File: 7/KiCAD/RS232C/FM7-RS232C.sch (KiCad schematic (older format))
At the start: 31 parts, among them CN2 DB9_Male, M10 74LS04, M11 8251A, M12 74LS27, M13 74LS11, M2 74LS38, M3 75188, M4 75189, M5 74LS00, M6 74LS32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

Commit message: Rewiring to add COM0/COM2 choice.
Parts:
- added unit 1 of M5
- added unit 1 of M6
- M6: footprint Package_DIP:DIP-14_W7.62mm_Socket -> (none)
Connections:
- net +5V: no longer M13.11
- net GNDPWR: now also M12.3; no longer M12.13
- net ~EIOS: now also M12.10; no longer M12.9
- net EAB0: now reaches CN_A1.1 (Pin_1), M11.12 (C/~D), M6.10
- net EAB2: now reaches CN_A1.2 (Pin_2), M13.1, M6.9
- net EAB4: now reaches CN_A1.3 (Pin_3), M12.2
- net EAB6: now reaches CN_A1.4 (Pin_4), M12.4
- net EAB6: now also M6.2
- net EAB1: now reaches CN_B1.1 (Pin_1), M13.2, M7.5
- net EAB1: now also M7.4
- net EAB3: now reaches CN_B1.2 (Pin_2), M12.1
- net EAB5: now reaches CN_B1.3 (Pin_3), M12.5
- net EAB5: now also M6.1
- net EAB7: now reaches CN_B1.4 (Pin_4)
- net EAB7: now also M12.13; no longer M12.3
- net at M6.8: now also M12.9; no longer M12.11
- net at M7.6: now also M12.11; no longer M12.10
- net at M13.12: now also M13.5; no longer M13.4
- removed net AB34: M12.12, M13.3, M7.4
- removed net AB567: M12.6, M13.5, M7.3
- net ~ERQ renamed ~ERW
- net ~ERW: now also M13.11; no longer M7.1
- new net: M5.3, M7.1
- new net: M5.1, M5.2, M6.3
- new net AB347: M12.12, M13.4, M7.3
- new net AB56: M12.6, M13.3
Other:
- note added: "+5V"
- note added: "=0 if AB02=0"
- note added: "=0 if IOS (FDxx)"
- note added: "=0\nif AB347=0,AB0=1"
- note added: "AB1=1"
- note added: "AB347=0"
- note added: "AB56=0"
- note added: "All Input=1 \nif FD02"
- note added: "GND"
- moved on the sheet: M7B
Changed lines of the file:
@@
 EESchema Schematic File Version 4
-LIBS:FM7-RS232C-cache
-EELAYER 26 0
+EELAYER 30 0
 EELAYER END
 $Descr A0 46811 33110
@@
 F 0 "M6" H 11100 9525 50  0000 C CNN
 F 1 "74LS32" H 11100 9434 50  0000 C CNN
-F 2 "Package_DIP:DIP-14_W7.62mm_Socket" H 11100 9200 50  0001 C CNN
+F 2 "" H 11100 9200 50  0001 C CNN
 F 3 "http://www.ti.com/lit/gpn/sn74LS32" H 11100 9200 50  0001 C CNN
 	3    11100 9200
@@
 L 74xx:74LS10 M7
 U 2 1 5C0782CB
-P 11100 9900
-F 0 "M7" H 11100 10225 50  0000 C CNN
-F 1 "74LS10" H 11100 10134 50  0000 C CNN
-F 2 "Package_DIP:DIP-14_W7.62mm_Socket" H 11100 9900 50  0001 C CNN
-F 3 "http://www.ti.com/lit/gpn/sn74LS10" H 11100 9900 50  0001 C CNN
-	2    11100 9900
+P 11100 10000
+F 0 "M7" H 11100 10325 50  0000 C CNN
+F 1 "74LS10" H 11100 10234 50  0000 C CNN
+F 2 "Package_DIP:DIP-14_W7.62mm_Socket" H 11100 10000 50  0001 C CNN
+F 3 "http://www.ti.com/lit/gpn/sn74LS10" H 11100 10000 50  0001 C CNN
+	2    11100 10000
 	1    0    0    -1
 $EndComp
@@
 F 0 "M6" H 11100 11825 50  0000 C CNN
 F 1 "74LS32" H 11100 11734 50  0000 C CNN
-F 2 "Package_DIP:DIP-14_W7.62mm_Socket" H 11100 11500 50  0001 C CNN
+F 2 "" H 11100 11500 50  0001 C CNN
 F 3 "http://www.ti.com/lit/gpn/sn74LS32" H 11100 11500 50  0001 C CNN
 	4    11100 11500
@@
 +5V
 Wire Wire Line
-	11400 9900 11750 9900
-Wire Wire Line
 	12350 9900 12600 9900
 Wire Wire Line
@@
 	12550 10000 12600 10000
 Wire Wire Line
-	8050 10600 10700 10600
-Wire Wire Line
-	5100 10500 10550 10500
-Wire Wire Line
-	10550 10500 10550 11600
-Wire Wire Line
-	10550 11600 10800 11600
-Connection ~ 10550 10500
-Wire Wire Line
-	10550 10500 10800 10500
-Wire Wire Line
-	10700 10600 10700 11400
-Wire Wire Line
-	10700 11400 10800 11400
-Connection ~ 10700 10600
-Wire Wire Line
-	10700 10600 10800 10600
-Wire Wire Line
-	10350 18600 10350 10700
-Wire Wire Line
-	10350 10700 10800 10700
-Wire Wire Line
-	11400 9200 11450 9200
-Wire Wire Line
-	11450 9200 11450 10000
-Wire Wire Line
-	11450 10000 11750 10000
+	8050 10600 10550 10600
+Wire Wire Line
+	5100 10500 10300 10500
+Wire Wire Line
+	10300 10500 10300 11600
+Wire Wire Line
+	10300 11600 10800 11600
+Connection ~ 10300 10500
+Wire Wire Line
+	10300 10500 10800 10500
+Wire Wire Line
+	10550 10600 10550 11400
+Wire Wire Line
+	10550 11400 10800 11400
+Connection ~ 10550 10600
+Wire Wire Line
+	10550 10600 10800 10600
+Wire Wire Line
+	11400 9200 11650 9200
+Wire Wire Line
+	11650 9200 11650 9800
 Wire Wire Line
 	3700 11600 4100 11600
@@
 Wire Wire Line
 	6950 11900 6950 8050
-Text Notes 6950 6650 0    50   ~ 0
+Text Notes 6950 6700 0    50   ~ 0
 EAB0
-Text Notes 6950 6850 0    50   ~ 0
+Text Notes 6950 6900 0    50   ~ 0
 EAB2
-Text Notes 6950 7050 0    50   ~ 0
+Text Notes 6950 7100 0    50   ~ 0
 EAB4
-Text Notes 6950 7250 0    50   ~ 0
+Text Notes 6950 7300 0    50   ~ 0
 EAB6
-Text Notes 7000 7450 0    50   ~ 0
+Text Notes 7600 7450 0    50   ~ 0
 EAB1
-Text Notes 7000 7650 0    50   ~ 0
+Text Notes 7600 7650 0    50   ~ 0
 EAB3
-Text Notes 7000 7850 0    50   ~ 0
+Text Notes 7600 7850 0    50   ~ 0
 EAB5
-Text Notes 7000 8050 0    50   ~ 0
+Text Notes 7600 8050 0    50   ~ 0
 EAB7
 Wire Wire Line
@@
 	4800 12800 4800 17500
 Wire Wire Line
-	8750 7450 8750 10000
-Wire Wire Line
-	8750 10000 10800 10000
-Connection ~ 10350 18600
+	8750 7450 8750 10100
+Wire Wire Line
+	8750 10100 10650 10100
 Wire Wire Line
 	6850 18600 7700 18600
@@
 Wire Wire Line
 	5200 9450 11550 9450
-Wire Wire Line
-	11550 9450 11550 9800
-Wire Wire Line
-	11550 9800 11750 9800
 Connection ~ 7400 19700
 Connection ~ 11500 19700
@@
 	12300 6700 14700 6700
 Wire Wire Line
-	6900 7850 12300 7850
-Wire Wire Line
-	12400 8050 12400 6500
-Wire Wire Line
-	12400 6500 14700 6500
-Wire Wire Line
-	6950 8050 12400 8050
+	6900 7850 9800 7850
+Wire Wire Line
+	12750 8050 12750 7200
+Wire Wire Line
+	6950 8050 12750 8050
 Wire Wire Line
 	12200 7300 12200 6600
@@
 	12200 6600 14700 6600
 Wire Wire Line
-	4250 7300 12200 7300
+	4250 7300 9400 7300
 Wire Wire Line
 	12600 7650 12600 7000
 Wire Wire Line
 	6850 7650 12600 7650
-Wire Wire Line
-	13850 7200 13850 19700
 Connection ~ 13850 19700
 Wire Wire Line
@@
 Wire Wire Line
 	9100 6900 13550 6900
-Wire Wire Line
-	14700 7200 13850 7200
 Wire Wire Line
 	12600 7000 14700 7000
@@
 	15300 7100 15400 7100
 Wire Wire Line
-	15400 7100 15400 7550
-Wire Wire Line
-	15400 7550 15750 7550
+	15400 7100 15400 7650
 Wire Wire Line
 	15300 6600 15650 6600
 Wire Wire Line
-	15650 6600 15650 7750
-Wire Wire Line
-	15650 7750 15750 7750
+	15650 6600 15650 7550
 Wire Wire Line
 	15400 7100 15400 4200
 Connection ~ 15400 7100
 Wire Wire Line
-	15650 6600 15650 3900
-Connection ~ 15650 6600
-Wire Wire Line
 	15250 8100 15400 8100
 Wire Wire Line
-	15400 8100 15400 7650
-Wire Wire Line
-	15400 7650 15750 7650
+	15400 8100 15400 7750
 Wire Wire Line
 	15400 4200 10500 4200
-Wire Wire Line
-	15650 3900 10100 3900
-Wire Wire Line
-	10100 3900 10100 9800
-Text Label 13450 3900 0    50   ~ 0
-AB567
+Text Label 15650 6800 0    50   ~ 0
+AB56
 Text Label 13450 4200 0    50   ~ 0
-AB34
-Wire Wire Line
-	10100 9800 10800 9800
+AB347
 Wire Wire Line
 	10500 4200 10500 9900
@@
 	16250 11850 16900 11850
 Wire Wire Line
-	16250 11850 16250 9050
-Wire Wire Line
-	16250 9050 12400 9050
-Wire Wire Line
-	12400 9050 12400 9800
-Wire Wire Line
-	12400 9800 12600 9800
+	16250 11850 16250 10600
+Wire Wire Line
+	16250 10600 13200 10600
+Wire Wire Line
+	12550 9800 12600 9800
 Connection ~ 16250 11850
-Text Label 15250 9050 0    50   ~ 0
-~ERQ
+Text Label 15250 10600 0    50   ~ 0
+~ERW
 $Comp
 L 74xx:74LS04 M10
@@
 	7600 16250 15600 16250
 Connection ~ 7500 12300
-Wire Wire Line
-	13200 9900 13500 9900
-Wire Wire Line
-	13500 9900 13500 16450
 Text Label 13250 9900 0    50   ~ 0
 ~WFD02
-Wire Wire Line
-	13500 16450 15600 16450
 Wire Wire Line
 	11400 11500 16900 11500
@@
 F 0 "M6" H 9430 19246 50  0000 L CNN
 F 1 "74LS32" H 9430 19155 50  0000 L CNN
-F 2 "Package_DIP:DIP-14_W7.62mm_Socket" H 9200 19200 50  0001 C CNN
+F 2 "" H 9200 19200 50  0001 C CNN
 F 3 "http://www.ti.com/lit/gpn/sn74LS32" H 9200 19200 50  0001 C CNN
 	5    9200 19200
@@
 	9200 18600 10000 18600
 Connection ~ 10000 18600
-Wire Wire Line
-	10000 18600 10350 18600
-Wire Wire Line
-	10350 18600 10750 18600
 Connection ~ 10750 19700
 Wire Wire Line
@@
 Text Label 7050 12400 0    50   ~ 0
 EE
+Text Label 6600 6700 0    50   ~ 0
+EAB0
+Text Label 6600 6900 0    50   ~ 0
+EAB2
+Text Label 6600 7100 0    50   ~ 0
+EAB4
+Text Label 6600 7300 0    50   ~ 0
+EAB6
+Text Label 7050 7450 0    50   ~ 0
+EAB1
+Text Label 7050 7650 0    50   ~ 0
+EAB3
+Text Label 7050 7850 0    50   ~ 0
+EAB5
+Text Label 7050 8050 0    50   ~ 0
+EAB7
+Text Notes 14550 8300 0    50   ~ 0
++5V
+Text Notes 14050 6500 0    50   ~ 0
+GND
+Wire Wire Line
+	12750 7200 14700 7200
+Wire Wire Line
+	14700 6500 13850 6500
+Wire Wire Line
+	13850 6500 13850 19700
+Wire Wire Line
+	15650 7550 15750 7550
+Wire Wire Line
+	15400 7650 15750 7650
+Wire Wire Line
+	15400 7750 15750 7750
+Wire Wire Line
+	11750 9800 11650 9800
+Wire Wire Line
+	11550 9900 11750 9900
+Wire Wire Line
+	11550 9450 11550 9900
+Wire Wire Line
+	11400 10000 11750 10000
+Text Notes 10500 9900 0    50   ~ 0
+AB347=0
+Text Notes 10300 10100 0    50   ~ 0
+AB1=1
+Text Notes 11300 10150 0    50   ~ 0
+=0\nif AB347=0,AB0=1
+Text Notes 11400 9200 0    50   ~ 0
+=0 if AB02=0
+Text Notes 10750 9450 0    50   ~ 0
+=0 if IOS (FDxx)
+Wire Wire Line
+	13700 9900 13700 16450
+Wire Wire Line
+	13200 9900 13700 9900
+Wire Wire Line
+	13700 16450 15600 16450
+Text Notes 12750 10250 0    50   ~ 0
+All Input=1 \nif FD02
+Wire Wire Line
+	13200 10600 13200 10950
+Wire Wire Line
+	13200 10950 10750 10950
+Wire Wire Line
+	10000 18600 10750 18600
+Wire Wire Line
+	10750 10700 10800 10700
+Wire Wire Line
+	10750 10700 10750 10950
+$Comp
+L 74xx:74LS32 M6
+U 1 1 621B650C
+P 11100 8550
+F 0 "M6" H 11100 8875 50  0000 C CNN
+F 1 "74LS32" H 11100 8784 50  0000 C CNN
+F 2 "" H 11100 8550 50  0001 C CNN
+F 3 "http://www.ti.com/lit/gpn/sn74LS32" H 11100 8550 50  0001 C CNN
+	1    11100 8550
+	1    0    0    -1
+$EndComp
+$Comp
+L 74xx:74LS00 M5
+U 1 1 621B9524
+P 12050 8550
+F 0 "M5" H 12050 8875 50  0000 C CNN
+F 1 "74LS00" H 12050 8784 50  0000 C CNN
+F 2 "" H 12050 8550 50  0001 C CNN
+F 3 "http://www.ti.com/lit/gpn/sn74ls00" H 12050 8550 50  0001 C CNN
+	1    12050 8550
+	1    0    0    -1
+$EndComp
+Wire Wire Line
+	11400 8550 11600 8550
+Wire Wire Line
+	11600 8550 11600 8450
+Wire Wire Line
+	11600 8450 11750 8450
+Wire Wire Line
+	11600 8550 11600 8650
+Wire Wire Line
+	11600 8650 11750 8650
+Connection ~ 11600 8550
+Wire Wire Line
+	12350 8550 12550 8550
+Wire Wire Line
+	12550 8550 12550 9800
+Wire Wire Line
+	9800 7850 9800 8450
+Wire Wire Line
+	9800 8450 10800 8450
+Connection ~ 9800 7850
+Wire Wire Line
+	9800 7850 12300 7850
+Wire Wire Line
+	9400 7300 9400 8650
+Wire Wire Line
+	9400 8650 10800 8650
+Connection ~ 9400 7300
+Wire Wire Line
+	9400 7300 12200 7300
+Text Notes 12350 8550 0    50   ~ 0
+AB56=0
+Wire Wire Line
+	10800 10000 10650 10000
+Wire Wire Line
+	10650 10000 10650 10100
+Connection ~ 10650 10100
+Wire Wire Line
+	10650 10100 10800 10100
 $EndSCHEMATC

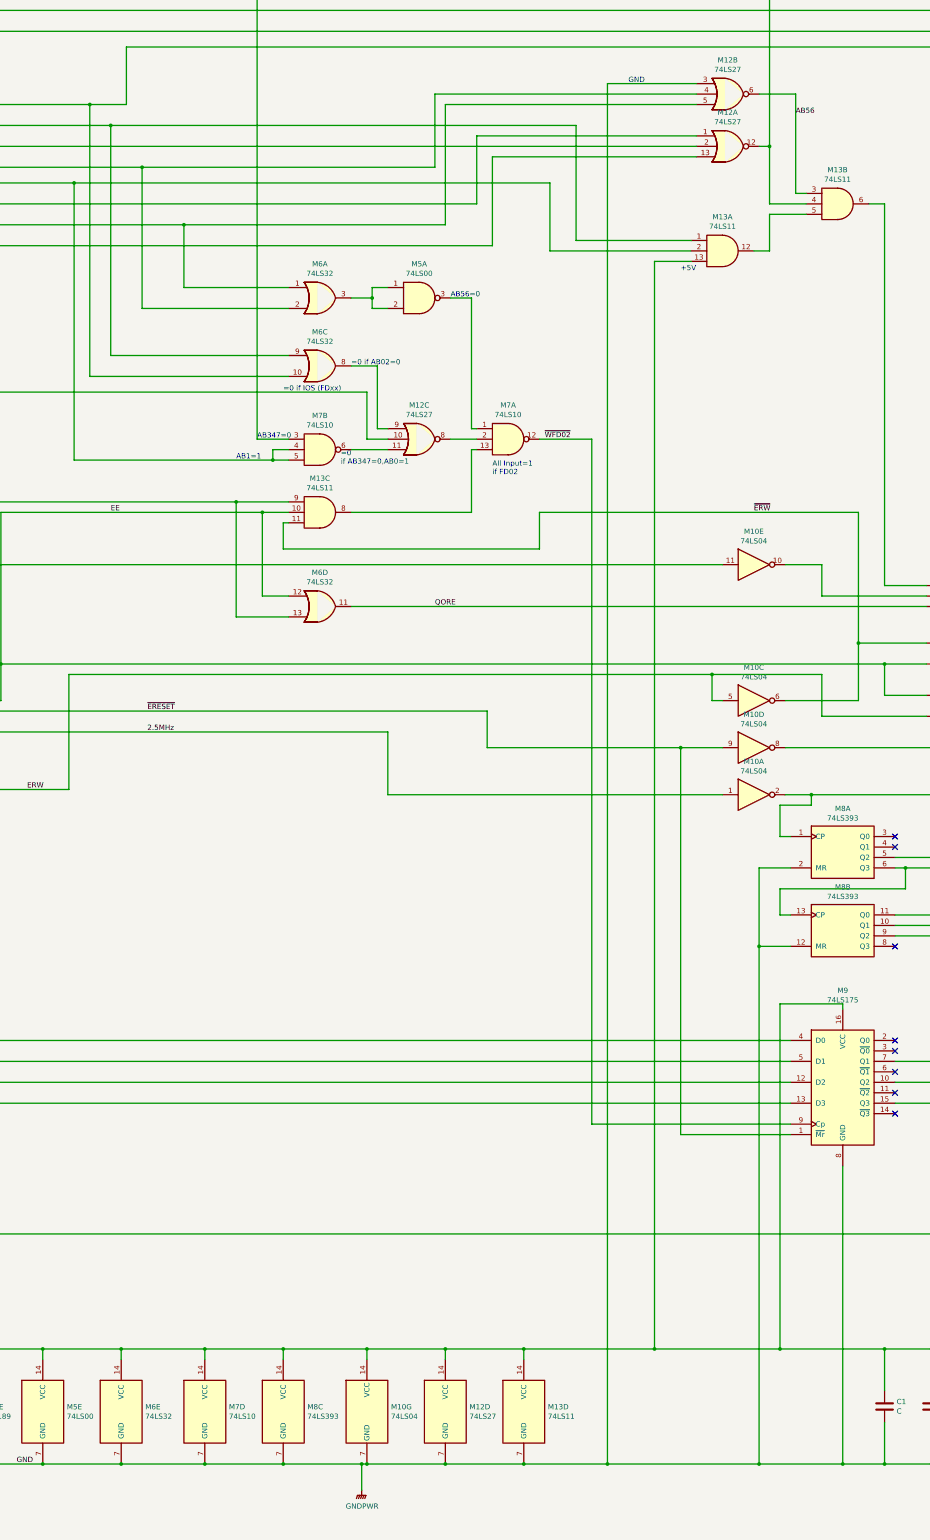
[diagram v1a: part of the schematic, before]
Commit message: Rewiring to add COM0/COM1 switching.
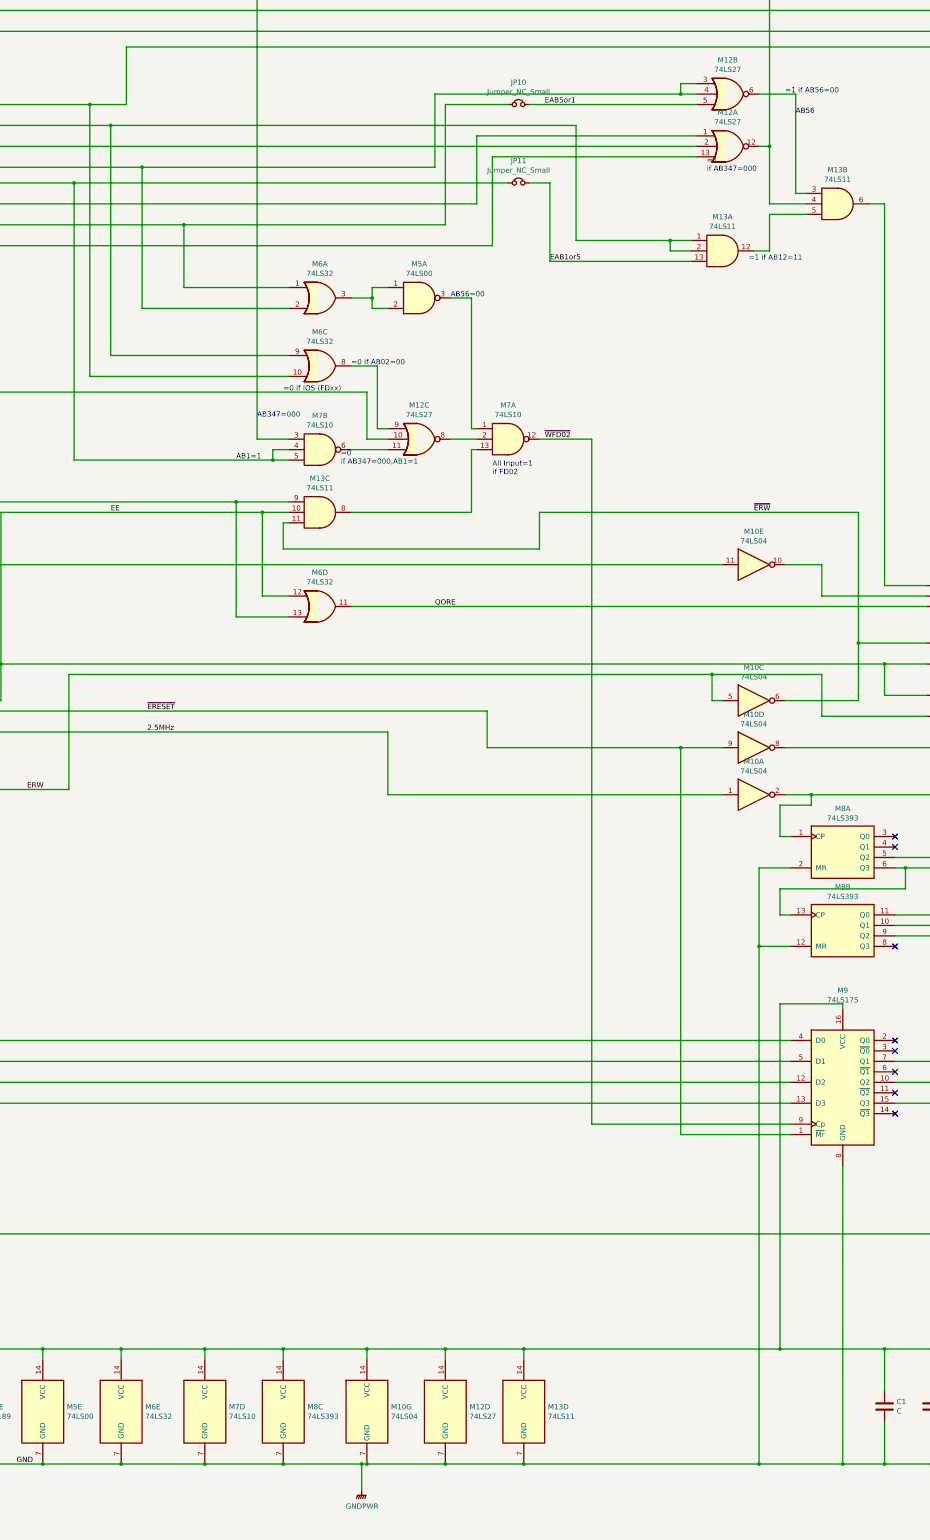
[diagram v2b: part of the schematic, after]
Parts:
- added JP10, JP11: Jumper_NC_Small, symbol Device:Jumper_NC_Small
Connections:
- net +5V: no longer M13.13
- net EAB1: now also JP11.1; no longer M13.2
- net EAB2: now also M13.2
- net EAB5: now also JP10.1; no longer M12.5
- net EAB6: now also M12.3
- net GNDPWR: no longer M12.3
- new net EAB1or5: JP11.2, M13.13
- new net EAB5or1: JP10.2, M12.5
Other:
- note added: "=0 if AB02=00"
- note added: "=0\nif AB347=000,AB1=1"
- note added: "=1 if AB12=11"
- note added: "=1 if AB56=00"
- note added: "=1\nif AB347=000"
- note added: "AB347=000"
- note added: "AB56=00"
- note removed: "+5V"
- note removed: "=0 if AB02=0"
- note removed: "=0\nif AB347=0,AB0=1"
- note removed: "AB347=0"
- note removed: "AB56=0"
- note removed: "GND"
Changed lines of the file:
@@
 	12300 7850 12300 6700
 Wire Wire Line
-	12300 6700 14700 6700
+	12300 6700 12900 6700
 Wire Wire Line
 	6900 7850 9800 7850
@@
 	6950 8050 12750 8050
 Wire Wire Line
-	12200 7300 12200 6600
-Wire Wire Line
-	12200 6600 14700 6600
-Wire Wire Line
 	4250 7300 9400 7300
 Wire Wire Line
@@
 Wire Wire Line
 	6850 7650 12600 7650
-Connection ~ 13850 19700
-Wire Wire Line
-	13300 7450 13300 8100
-Wire Wire Line
-	13300 8100 14650 8100
-Wire Wire Line
-	8750 7450 13300 7450
+Wire Wire Line
+	13300 7450 13300 8200
+Wire Wire Line
+	8750 7450 12900 7450
 Wire Wire Line
 	13550 6900 13550 8000
 Wire Wire Line
-	13550 8000 14650 8000
+	13550 8000 14450 8000
 Wire Wire Line
 	9100 6900 13550 6900
 Wire Wire Line
 	12600 7000 14700 7000
-Wire Wire Line
-	14650 8200 14300 8200
-Wire Wire Line
-	14300 8200 14300 18600
-Connection ~ 14300 18600
 Wire Wire Line
 	9250 6700 9250 6150
@@
 Connection ~ 13050 19700
 Wire Wire Line
-	13050 19700 13850 19700
-Wire Wire Line
 	16100 19700 16500 19700
 Wire Wire Line
@@
 Wire Wire Line
 	17350 19700 17800 19700
-Wire Wire Line
-	13050 18600 14300 18600
-Wire Wire Line
-	14300 18600 15500 18600
-Wire Wire Line
-	13850 19700 15300 19700
 Wire Wire Line
 	7700 18800 7700 18600
@@
 Text Label 7050 8050 0    50   ~ 0
 EAB7
-Text Notes 14550 8300 0    50   ~ 0
-+5V
-Text Notes 14050 6500 0    50   ~ 0
-GND
 Wire Wire Line
 	12750 7200 14700 7200
 Wire Wire Line
-	14700 6500 13850 6500
-Wire Wire Line
-	13850 6500 13850 19700
+	14700 6500 14550 6500
 Wire Wire Line
 	15650 7550 15750 7550
@@
 Wire Wire Line
 	11400 10000 11750 10000
-Text Notes 10500 9900 0    50   ~ 0
-AB347=0
+Text Notes 10500 9700 0    50   ~ 0
+AB347=000
 Text Notes 10300 10100 0    50   ~ 0
 AB1=1
 Text Notes 11300 10150 0    50   ~ 0
-=0\nif AB347=0,AB0=1
+=0\nif AB347=000,AB1=1
 Text Notes 11400 9200 0    50   ~ 0
-=0 if AB02=0
+=0 if AB02=00
 Text Notes 10750 9450 0    50   ~ 0
 =0 if IOS (FDxx)
@@
 	9400 7300 12200 7300
 Text Notes 12350 8550 0    50   ~ 0
-AB56=0
+AB56=00
 Wire Wire Line
 	10800 10000 10650 10000
@@
 Wire Wire Line
 	10650 10100 10800 10100
+Wire Wire Line
+	12200 6600 14550 6600
+Wire Wire Line
+	12200 7300 12200 6600
+$Comp
+L Device:Jumper_NC_Small JP10
+U 1 1 62352C12
+P 13000 6700
+F 0 "JP10" H 13000 6912 50  0000 C CNN
+F 1 "Jumper_NC_Small" H 13000 6821 50  0000 C CNN
+F 2 "" H 13000 6700 50  0001 C CNN
+F 3 "~" H 13000 6700 50  0001 C CNN
+	1    13000 6700
+	1    0    0    -1
+$EndComp
+$Comp
+L Device:Jumper_NC_Small JP11
+U 1 1 62352F76
+P 13000 7450
+F 0 "JP11" H 13000 7662 50  0000 C CNN
+F 1 "Jumper_NC_Small" H 13000 7571 50  0000 C CNN
+F 2 "" H 13000 7450 50  0001 C CNN
+F 3 "~" H 13000 7450 50  0001 C CNN
+	1    13000 7450
+	1    0    0    -1
+$EndComp
+Wire Wire Line
+	13100 6700 14700 6700
+Wire Wire Line
+	13100 7450 13300 7450
+Text Label 13300 8200 0    50   ~ 0
+EAB1or5
+Text Label 13250 6700 0    50   ~ 0
+EAB5or1
+Text Notes 15550 6600 0    50   ~ 0
+=1 if AB56=00
+Text Notes 14800 7350 0    50   ~ 0
+           =1\nif AB347=000
+Text Notes 15200 8200 0    50   ~ 0
+=1 if AB12=11
+Wire Wire Line
+	13300 8200 14650 8200
+Wire Wire Line
+	13050 18600 15500 18600
+Wire Wire Line
+	14450 8000 14450 8100
+Wire Wire Line
+	14450 8100 14650 8100
+Connection ~ 14450 8000
+Wire Wire Line
+	14450 8000 14650 8000
+Wire Wire Line
+	13050 19700 15300 19700
+Wire Wire Line
+	14550 6500 14550 6600
+Connection ~ 14550 6600
+Wire Wire Line
+	14550 6600 14700 6600
 $EndSCHEMATC

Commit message: Assigned footprints
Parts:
- JP10, JP11: footprint (none) -> Connector_PinHeader_2.54mm:PinHeader_1x02_P2.54mm_Vertical
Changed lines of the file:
@@
 F 0 "JP10" H 13000 6912 50  0000 C CNN
 F 1 "Jumper_NC_Small" H 13000 6821 50  0000 C CNN
-F 2 "" H 13000 6700 50  0001 C CNN
+F 2 "Connector_PinHeader_2.54mm:PinHeader_1x02_P2.54mm_Vertical" H 13000 6700 50  0001 C CNN
 F 3 "~" H 13000 6700 50  0001 C CNN
 	1    13000 6700
@@
 F 0 "JP11" H 13000 7662 50  0000 C CNN
 F 1 "Jumper_NC_Small" H 13000 7571 50  0000 C CNN
-F 2 "" H 13000 7450 50  0001 C CNN
+F 2 "Connector_PinHeader_2.54mm:PinHeader_1x02_P2.54mm_Vertical" H 13000 7450 50  0001 C CNN
 F 3 "~" H 13000 7450 50  0001 C CNN
 	1    13000 7450

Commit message: Updated PCB
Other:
- note added: "=1 if AB56=00 and AB12=11 and AB347=0"
- note added: "=1 if all input=0"
- note removed: "AB56=00"
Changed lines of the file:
@@
 	9400 7300 12200 7300
 Text Notes 12350 8550 0    50   ~ 0
-AB56=00
+=1 if AB56=00
 Wire Wire Line
 	10800 10000 10650 10000
@@
 Wire Wire Line
 	14550 6600 14700 6600
+Text Notes 12400 9900 1    50   ~ 0
+=1 if all input=0
+Text Notes 16500 9400 1    50   ~ 0
+=1 if AB56=00 and AB12=11 and AB347=0
 $EndSCHEMATC

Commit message: Added comment.
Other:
- note added: "~WFD02~=\nAB=00000010 and\n~IOS~=0 (IOS=1) and\nEE=1 and\nEQ=1 and\n~ERW~=1 (ERW=0)\n"
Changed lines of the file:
@@
 Text Notes 16500 9400 1    50   ~ 0
 =1 if AB56=00 and AB12=11 and AB347=0
+Text Notes 13750 10050 0    50   ~ 0
+~WFD02~=\nAB=00000010 and\n~IOS~=0 (IOS=1) and\nEE=1 and\nEQ=1 and\n~ERW~=1 (ERW=0)\n
 $EndSCHEMATC

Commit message: Fixed error in comment.
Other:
- note added: "WFD02=\nAB=00000010 and\n~IOS~=0 (IOS=1) and\nEE=1 and\nEQ=1 and\n~ERW~=1 (ERW=0)\n"
- note removed: "~WFD02~=\nAB=00000010 and\n~IOS~=0 (IOS=1) and\nEE=1 and\nEQ=1 and\n~ERW~=1 (ERW=0)\n"
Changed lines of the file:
@@
 =1 if AB56=00 and AB12=11 and AB347=0
 Text Notes 13750 10050 0    50   ~ 0
-~WFD02~=\nAB=00000010 and\n~IOS~=0 (IOS=1) and\nEE=1 and\nEQ=1 and\n~ERW~=1 (ERW=0)\n
+WFD02=\nAB=00000010 and\n~IOS~=0 (IOS=1) and\nEE=1 and\nEQ=1 and\n~ERW~=1 (ERW=0)\n
 $EndSCHEMATC
